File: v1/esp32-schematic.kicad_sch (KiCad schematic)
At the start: 46 parts, among them J1 GN-2630G, J10 Screw_Terminal_01x04, J11 Screw_Terminal_01x04, J12 Screw_Terminal_01x04, J13 Screw_Terminal_01x04, J15 POWER, J2 Jumper, J3 Micro_SD_Card, J4 Screw_Terminal_01x04, J5 Screw_Terminal_01x04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

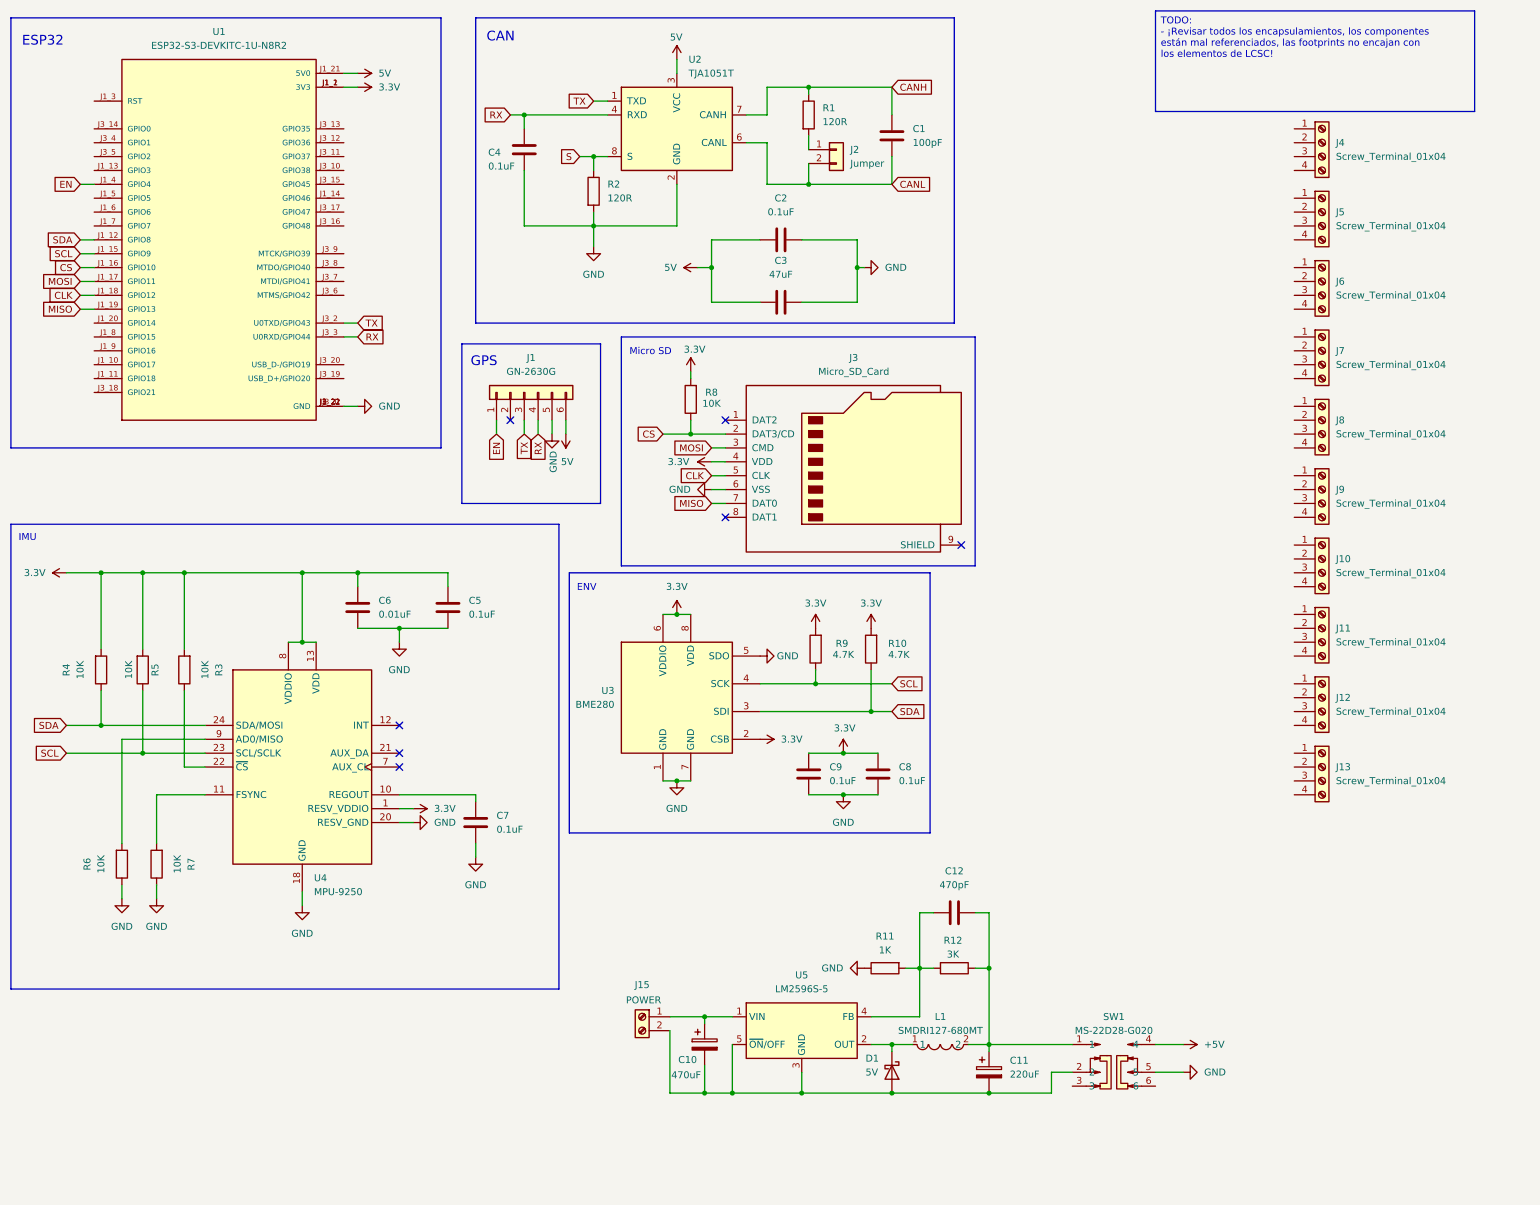
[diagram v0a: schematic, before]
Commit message: external power supply entry added, and todo list updated
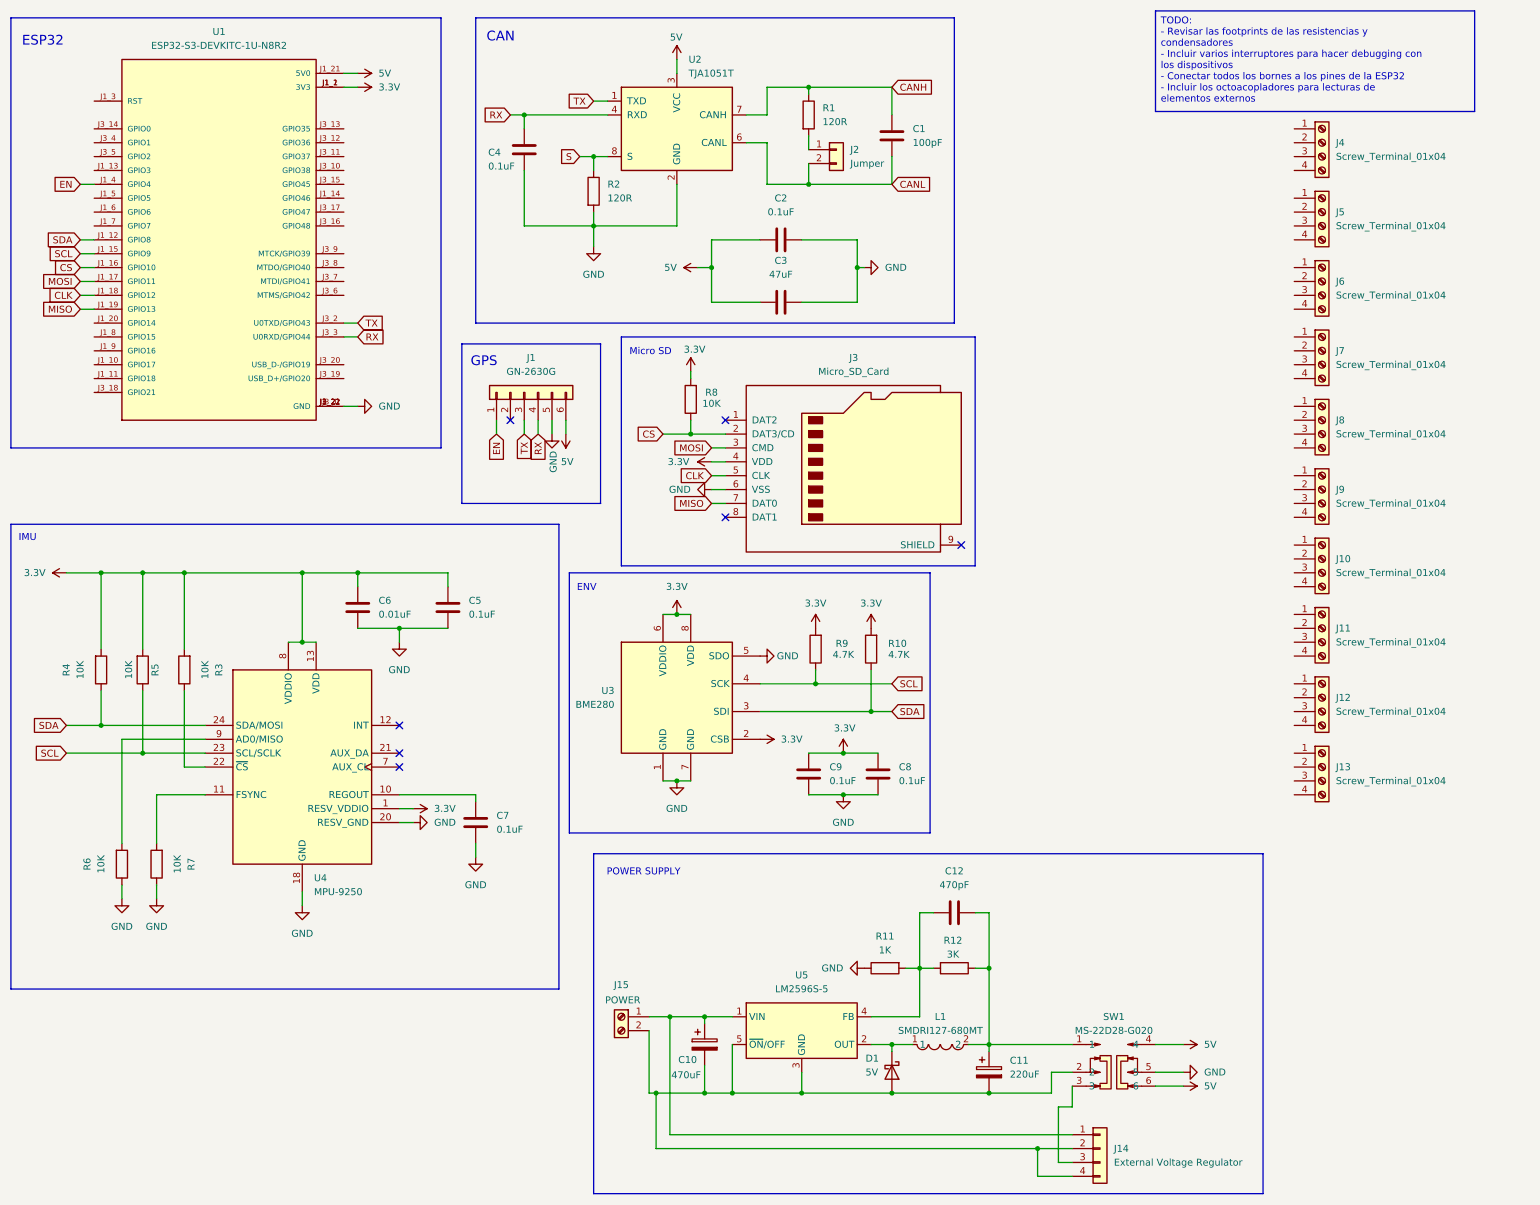
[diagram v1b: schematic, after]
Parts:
- added J14: External Voltage Regulator, Connector_PinHeader_2.54mm:PinHeader_1x04_P2.54mm_Vertical, symbol Connector_Generic:Conn_01x04
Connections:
- net +5V is gone; now on net 5V: SW1.4
- net 5V: now also SW1.6
- net at C10.1, J15.1 (Pin_1), U5.1 (VIN): now also J14.1 (Pin_1)
- net at C10.2, C11.2, D1.2 (A)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: now also J14.2 (Pin_2), J14.4 (Pin_4)
- net at SW1.3: now also J14.3 (Pin_3)
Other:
- note added: "POWER SUPPLY"
- moved on the sheet: J15
